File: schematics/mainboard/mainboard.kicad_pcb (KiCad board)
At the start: 4 copper layers, 99.5 x 193.5 mm, 106 parts, among them J1 SD_Card_Receptacle, J2 LCD_CONN, J3 USB_C_Receptacle_USB2.0_16P, J4 BATTERY_CONN, J5 527461671, J6 SPEAKER_CONN, J9 AudioJack3, P1 1-1473005-4, U1 AMS1117-3.3, U10 PCA9555PW, U2 AMS1117-3.3, U3 MAX3421EETJ_T, U5 AMS1117-1.8, U6 TPS63002, U7 BQ24072RGT, U9 TPS22917DBV, Y1 12MHz

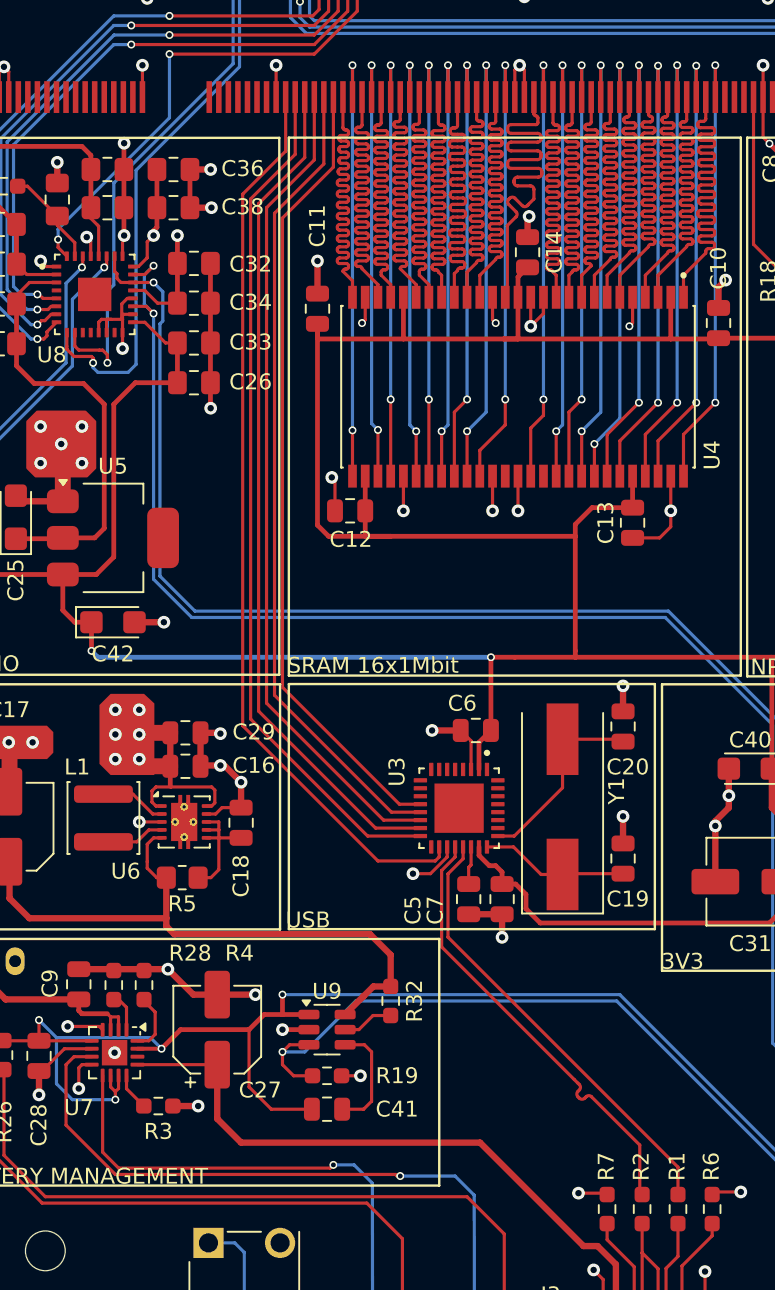
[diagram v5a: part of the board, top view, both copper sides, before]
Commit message: Incorrect part number and also incorrect footprint fixed. Another attempt at JLCPCB.
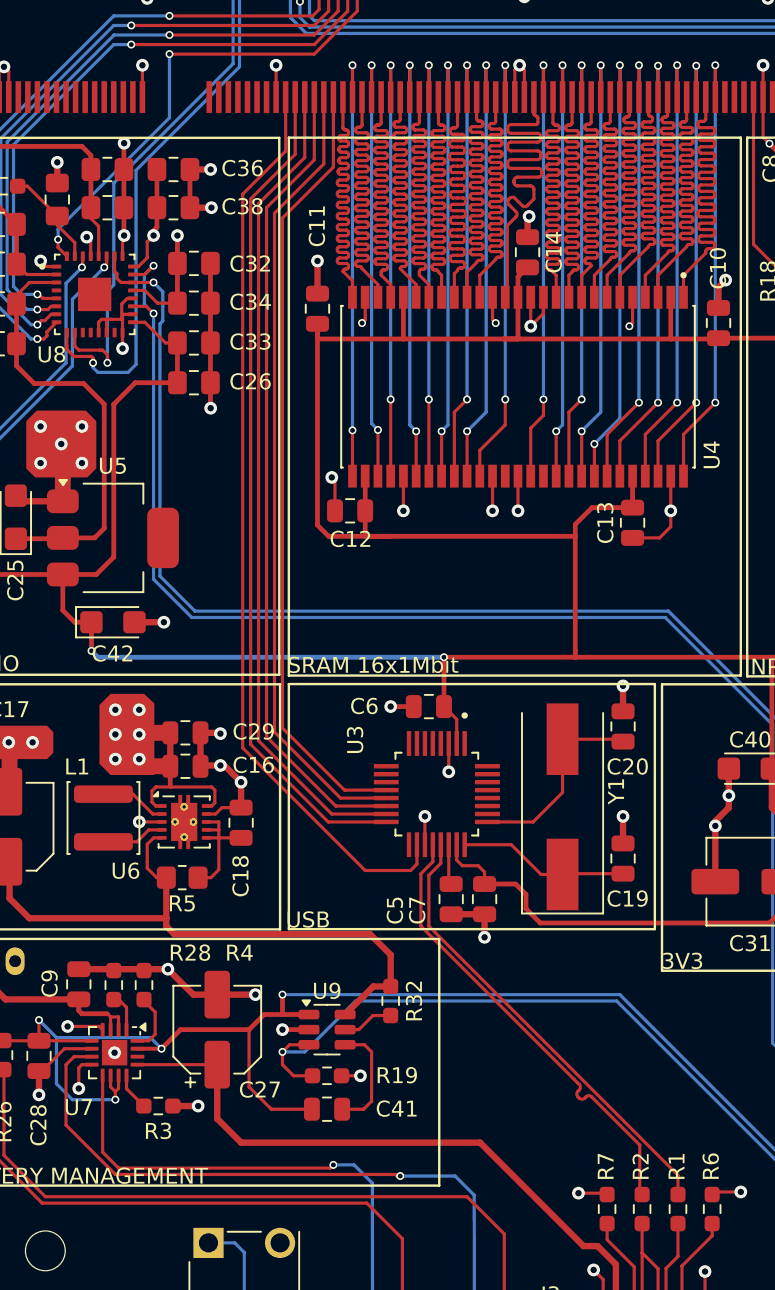
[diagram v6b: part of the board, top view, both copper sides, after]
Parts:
- U3: footprint MAX:QFN50P500X500X80-33N -> MAX2:QFP50P700X700X120-32N
- moved C6 3.31 mm to (154.6, 237.3)
- moved U3 1.66 mm to (155.1, 242.8)
- moved C5 1.10 mm to (156.0, 249.4)
- moved C7 1.10 mm to (158.1, 249.4)
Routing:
- net GND: track 253.7 -> 251.0 mm, vias 97 -> 98
- net USB_HCI_MOSI: track 54.0 -> 52.4 mm
- net USB_HCI_XI: track 9.29 -> 10.7 mm
- net USB_HCI_MISO: track 53.0 -> 51.6 mm
- net ~{USB_HCI_SS}: track 52.0 -> 50.8 mm
- net USB_HCI_SCLK: track 51.1 -> 49.9 mm
- net ~{USB_HCI_RESET}: track 50.1 -> 49.1 mm
- net Net-(U3-D-): track 28.0 -> 28.7 mm
- net Net-(U3-D+): track 28.1 -> 28.7 mm
